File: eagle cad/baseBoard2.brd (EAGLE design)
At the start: 100 x 69.5 mm, 75 parts

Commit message: .
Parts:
- added E$76: 100K, ref-packages:0207/12
- added E$77, E$78: (no value), testpad:P1-13
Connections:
- net GND: now also E$76.1
- net S$22: now also E$76.2
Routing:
- net S$22: track 43.5 -> 45.4 mm
- net GND: track 274.2 -> 275.8 mm
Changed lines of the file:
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@@
 <?xml version="1.0" encoding="utf-8"?>
 <!DOCTYPE eagle SYSTEM "eagle.dtd">
-<eagle version="8.2.2">
+<eagle version="9.6.2">
 <drawing>
 <settings>
 <setting alwaysvectorfont="no"/>
+<setting keepoldvectorfont="yes"/>
 <setting verticaltext="up"/>
 </settings>
-<grid distance="0.2" unitdist="mm" unit="mm" style="lines" multiple="1" display="yes" altdistance="0.003125" altunitdist="mic" altunit="mm"/>
+<grid distance="0.4" unitdist="mm" unit="mm" style="lines" multiple="1" display="yes" altdistance="0.003125" altunitdist="mic" altunit="mm"/>
 <layers>
 <layer number="1" name="Top" color="4" fill="1" visible="yes" active="yes"/>
@@
 <layer number="17" name="Pads" color="2" fill="1" visible="yes" active="yes"/>
 <layer number="18" name="Vias" color="2" fill="1" visible="yes" active="yes"/>
-<layer number="19" name="Unrouted" color="6" fill="1" visible="no" active="yes"/>
+<layer number="19" name="Unrouted" color="6" fill="1" visible="yes" active="yes"/>
 <layer number="20" name="Dimension" color="15" fill="1" visible="yes" active="yes"/>
-<layer number="21" name="tPlace" color="7" fill="1" visible="no" active="yes"/>
+<layer number="21" name="tPlace" color="7" fill="1" visible="yes" active="yes"/>
 <layer number="22" name="bPlace" color="7" fill="1" visible="no" active="yes"/>
-<layer number="23" name="tOrigins" color="15" fill="1" visible="no" active="yes"/>
-<layer number="24" name="bOrigins" color="15" fill="1" visible="no" active="yes"/>
+<layer number="23" name="tOrigins" color="15" fill="1" visible="yes" active="yes"/>
+<layer number="24" name="bOrigins" color="15" fill="1" visible="yes" active="yes"/>
 <layer number="25" name="tNames" color="7" fill="1" visible="no" active="yes"/>
 <layer number="26" name="bNames" color="7" fill="1" visible="no" active="yes"/>
-<layer number="27" name="tValues" color="7" fill="1" visible="no" active="yes"/>
+<layer number="27" name="tValues" color="7" fill="1" visible="yes" active="yes"/>
 <layer number="28" name="bValues" color="7" fill="1" visible="no" active="yes"/>
 <layer number="29" name="tStop" color="7" fill="3" visible="no" active="yes"/>
@@
 <param name="dpMaxLengthDifference" value="10mm"/>
 <param name="dpGapFactor" value="2.5"/>
-<param name="checkGrid" value="0"/>
 <param name="checkAngle" value="0"/>
 <param name="checkFont" value="1"/>
 <param name="checkRestrict" value="1"/>
+<param name="checkStop" value="0"/>
+<param name="checkValues" value="0"/>
+<param name="checkNames" value="1"/>
+<param name="checkWireStubs" value="1"/>
+<param name="checkPolygonWidth" value="0"/>
 <param name="useDiameter" value="13"/>
 <param name="maxErrors" value="50"/>
@@
 <attribute name="VALUE" x="89.2" y="22.6" size="0.0254" layer="27"/>
 </element>
+<element name="E$76" library="ref-packages" library_urn="urn:adsk.eagle:library:338" package="0207/12" value="100K" x="40.8" y="10.4" smashed="yes" rot="R90">
+<attribute name="NAME" x="39.403" y="7.225" size="1.27" layer="25" ratio="10" rot="R90"/>
+<attribute name="VALUE" x="41.4858" y="8.114" size="1.27" layer="27" ratio="10" rot="R90"/>
+</element>
+<element name="E$77" library="testpad" library_urn="urn:adsk.eagle:library:385" package="P1-13" value="" x="40.8" y="16.6" smashed="yes">
+<attribute name="NAME" x="39.784" y="17.87" size="1.27" layer="25" ratio="10"/>
+<attribute name="VALUE" x="40.8" y="16.6" size="0.0254" layer="27"/>
+</element>
+<element name="E$78" library="testpad" library_urn="urn:adsk.eagle:library:385" package="P1-13" value="" x="40.8" y="4.2" smashed="yes">
+<attribute name="NAME" x="39.784" y="5.47" size="1.27" layer="25" ratio="10"/>
+<attribute name="VALUE" x="40.8" y="4.2" size="0.0254" layer="27"/>
+</element>
 </elements>
 <signals>
@@
 <wire x1="58.07" y1="5.6" x2="64.302" y2="5.6" width="1.27" layer="16"/>
 <wire x1="20.62" y1="3.38" x2="21.42" y2="2.58" width="1.27" layer="16"/>
-<wire x1="45.09573125" y1="2.58" x2="21.42" y2="2.58" width="1.27" layer="16"/>
+<wire x1="45.09573125" y1="2.58" x2="41.2" y2="2.58" width="1.27" layer="16"/>
+<wire x1="41.2" y1="2.58" x2="21.42" y2="2.58" width="1.27" layer="16"/>
 <wire x1="45.09573125" y1="2.58" x2="45.13573125" y2="2.54" width="1.27" layer="16"/>
 <wire x1="45.2" y1="2.584" x2="51.6751625" y2="2.584" width="1.27" layer="16"/>
@@
 <wire x1="49.17" y1="19.3" x2="49.37" y2="19.1" width="1.7" layer="16" curve="4.255771"/>
 <wire x1="49.37" y1="19.1" x2="49.27" y2="14.4" width="1.7" layer="16"/>
-<wire x1="74.58" y1="5.73" x2="80.5" y2="16.05" width="0" layer="19" extent="16-16"/>
-<wire x1="64.302" y1="5.6" x2="63" y2="5.55" width="0" layer="19" extent="16-16"/>
+<contactref element="E$76" pad="1"/>
+<wire x1="40.8" y1="4.05" x2="40.8" y2="2.98" width="1.27" layer="16"/>
+<wire x1="40.8" y1="2.98" x2="41.2" y2="2.58" width="0.7" layer="16"/>
+<wire x1="74.58" y1="5.73" x2="80.5" y2="16.05" width="0" layer="19" extent="1-1"/>
+<wire x1="64.42" y1="5.73" x2="63" y2="5.55" width="0" layer="19" extent="16-16"/>
 </signal>
 <signal name="S$5">
@@
 <wire x1="85.9" y1="16.19" x2="85.9" y2="22.63" width="1.27" layer="16"/>
 <contactref element="E$20" pad="+"/>
-<wire x1="45.53" y1="10.16" x2="31.49" y2="10.16" width="1.27" layer="16"/>
+<wire x1="45.53" y1="9.76" x2="31.63" y2="9.76" width="1.27" layer="16"/>
+<wire x1="31.4" y1="9.99" x2="31.63" y2="9.76" width="1.27" layer="16"/>
 <contactref element="E$17" pad="1"/>
-<wire x1="31.49" y1="10.16" x2="31.4" y2="9.99" width="0.7" layer="16"/>
 <wire x1="46.63" y1="19.3" x2="46.63" y2="14.5" width="1.7" layer="16"/>
 <wire x1="46.63" y1="14.5" x2="46.73" y2="14.4" width="0.8128" layer="16"/>
 <wire x1="46.73" y1="14.4" x2="45.53" y2="13.2" width="1.27" layer="16"/>
-<wire x1="45.53" y1="13.2" x2="45.53" y2="10.16" width="1.27" layer="16"/>
+<wire x1="45.53" y1="13.2" x2="45.53" y2="9.76" width="1.27" layer="16"/>
 <wire x1="51.37" y1="39.6" x2="50.97" y2="39.2" width="1.27" layer="16"/>
 <wire x1="50.97" y1="39.2" x2="49.37" y2="37.6" width="1.27" layer="16"/>
@@
 <contactref element="E$46" pad="+"/>
 <contactref element="E$19" pad="4"/>
-<wire x1="45.2" y1="4.616" x2="43.606" y2="6.21" width="1.27" layer="16"/>
-<wire x1="43.606" y1="6.21" x2="28.8" y2="6.21" width="1.27" layer="16"/>
-<wire x1="39.00875" y1="12.8" x2="28.8" y2="12.8" width="1.27" layer="16"/>
-<wire x1="28.8" y1="12.8" x2="28.8" y2="6.21" width="1.27" layer="16"/>
-<wire x1="39.00875" y1="12.8" x2="39.01" y2="12.79" width="0.7" layer="16"/>
-<wire x1="39.01" y1="12.79" x2="39.01" y2="22.39" width="1.27" layer="16"/>
+<wire x1="45.2" y1="4.616" x2="43.006" y2="6.81" width="1.27" layer="16"/>
+<wire x1="43.006" y1="6.81" x2="28.8" y2="6.81" width="1.27" layer="16"/>
+<wire x1="37.40875" y1="12.8" x2="28.8" y2="12.8" width="1.27" layer="16"/>
+<wire x1="28.8" y1="12.8" x2="28.8" y2="6.81" width="1.27" layer="16"/>
+<wire x1="37.40875" y1="12.8" x2="37.41" y2="12.79" width="0.7" layer="16"/>
+<wire x1="37.41" y1="12.79" x2="38.2" y2="12.79" width="1.27" layer="16"/>
+<wire x1="38.2" y1="12.79" x2="38.2" y2="17.2" width="1.27" layer="16"/>
+<wire x1="38.2" y1="17.2" x2="38.2" y2="18" width="1.27" layer="16"/>
+<wire x1="38.2" y1="18" x2="39.01" y2="18.81" width="1.27" layer="16"/>
+<wire x1="39.01" y1="18.81" x2="39.01" y2="22.39" width="1.27" layer="16"/>
+<contactref element="E$76" pad="2"/>
+<wire x1="40.8" y1="16.75" x2="38.65" y2="16.75" width="1.27" layer="16"/>
+<wire x1="38.65" y1="16.75" x2="38.2" y2="17.2" width="0.7" layer="16"/>
 </signal>
 <signal name="S$10">
@@
 </signal>
 </signals>
+<mfgpreviewcolors>
+<mfgpreviewcolor name="soldermaskcolor" color="0xC8008000"/>
+<mfgpreviewcolor name="silkscreencolor" color="0xFFFEFEFE"/>
+<mfgpreviewcolor name="backgroundcolor" color="0xFF282828"/>
+<mfgpreviewcolor name="coppercolor" color="0xFFFFBF00"/>
+<mfgpreviewcolor name="substratecolor" color="0xFF786E46"/>
+</mfgpreviewcolors>
 </board>
 </drawing>
 <compatibility>
 <note version="8.2" severity="warning">
-Since Version 8.2, Eagle supports online libraries. The ids
+Since Version 8.2, EAGLE supports online libraries. The ids
 of those online libraries will not be understood (or retained)
 with this version.

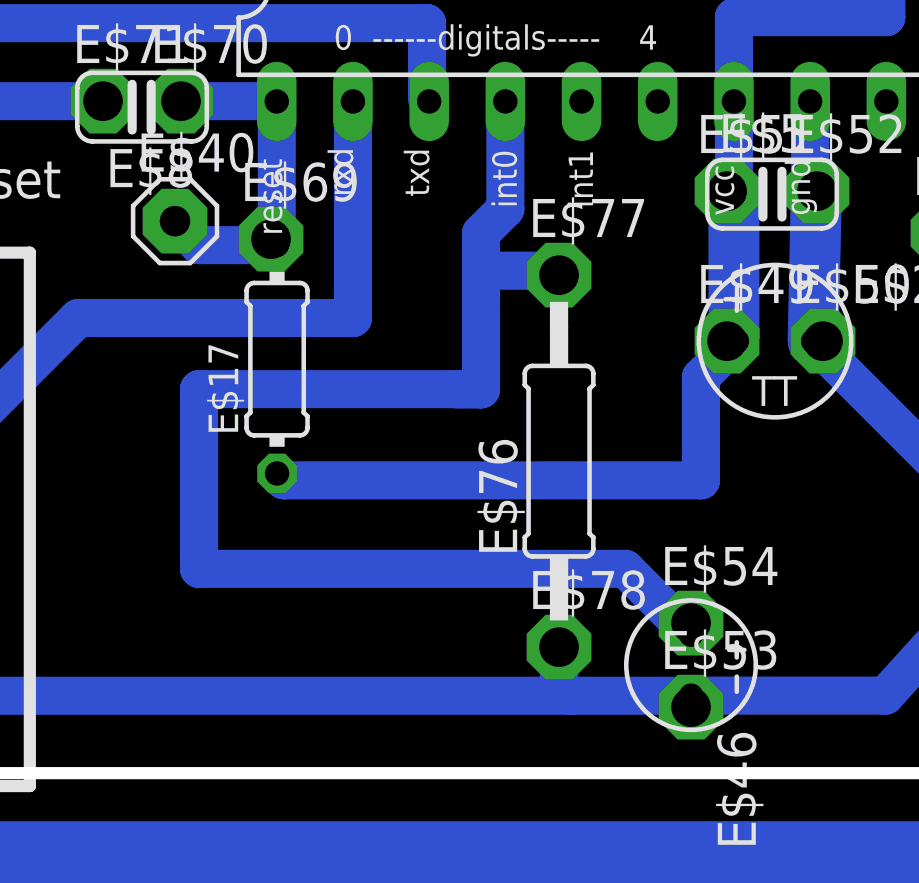
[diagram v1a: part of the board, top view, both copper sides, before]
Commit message: modified pullup resistor for interrupt
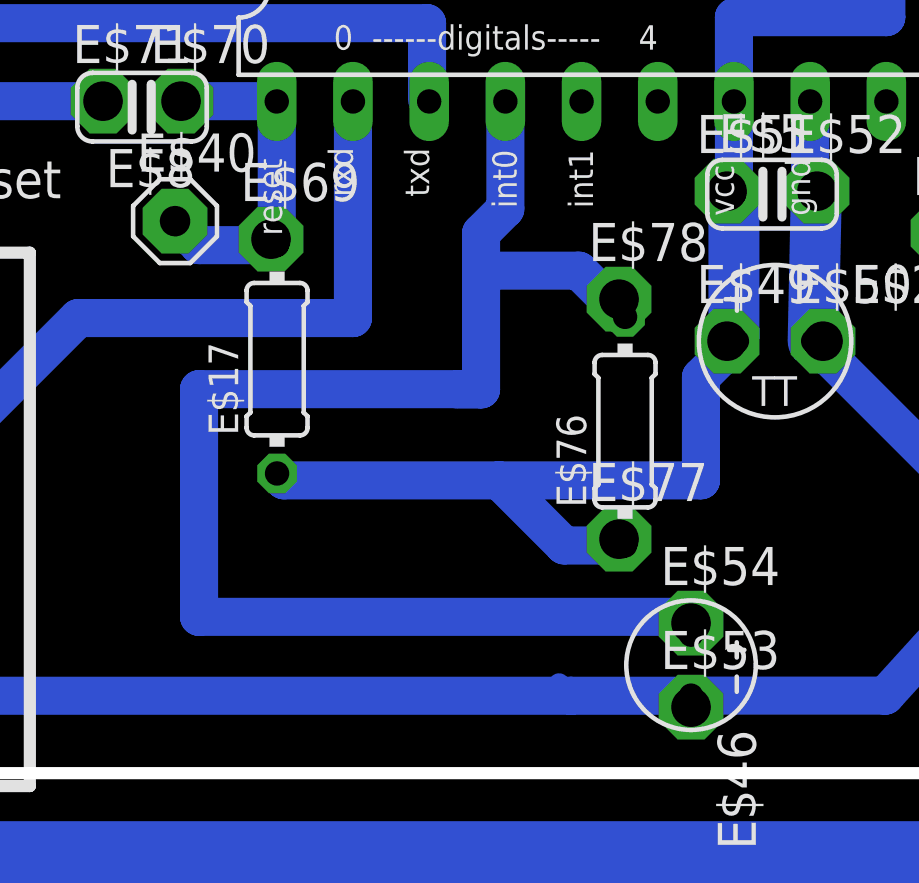
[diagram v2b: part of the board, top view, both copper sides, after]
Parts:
- E$76: value 100K -> 10k; device ref-packages:0207/12 -> eagle-ltspice:0204/7
- moved E$78 11.8 mm to (42.8, 15.8)
- moved E$77 9.02 mm to (42.8, 7.80)
- moved E$76 2.42 mm to (43.0, 11.4)
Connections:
- net GND: no longer E$76.1
- net VCC3.3V: now also E$76.1
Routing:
- net VCC3.3V: track 133.9 -> 139.0 mm
- net S$22: track 45.4 -> 49.2 mm
- net GND: track 275.8 -> 274.7 mm
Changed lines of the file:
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@@
 <attribute name="VALUE" x="89.2" y="22.6" size="0.0254" layer="27"/>
 </element>
-<element name="E$76" library="ref-packages" library_urn="urn:adsk.eagle:library:338" package="0207/12" value="100K" x="40.8" y="10.4" smashed="yes" rot="R90">
-<attribute name="NAME" x="39.403" y="7.225" size="1.27" layer="25" ratio="10" rot="R90"/>
-<attribute name="VALUE" x="41.4858" y="8.114" size="1.27" layer="27" ratio="10" rot="R90"/>
+<element name="E$77" library="testpad" library_urn="urn:adsk.eagle:library:385" package="P1-13" value="" x="42.8" y="7.8" smashed="yes">
+<attribute name="NAME" x="41.784" y="9.07" size="1.27" layer="25" ratio="10"/>
+<attribute name="VALUE" x="42.8" y="7.8" size="0.0254" layer="27"/>
 </element>
-<element name="E$77" library="testpad" library_urn="urn:adsk.eagle:library:385" package="P1-13" value="" x="40.8" y="16.6" smashed="yes">
-<attribute name="NAME" x="39.784" y="17.87" size="1.27" layer="25" ratio="10"/>
-<attribute name="VALUE" x="40.8" y="16.6" size="0.0254" layer="27"/>
+<element name="E$78" library="testpad" library_urn="urn:adsk.eagle:library:385" package="P1-13" value="" x="42.8" y="15.8" smashed="yes">
+<attribute name="NAME" x="41.784" y="17.07" size="1.27" layer="25" ratio="10"/>
+<attribute name="VALUE" x="42.8" y="15.8" size="0.0254" layer="27"/>
 </element>
-<element name="E$78" library="testpad" library_urn="urn:adsk.eagle:library:385" package="P1-13" value="" x="40.8" y="4.2" smashed="yes">
-<attribute name="NAME" x="39.784" y="5.47" size="1.27" layer="25" ratio="10"/>
-<attribute name="VALUE" x="40.8" y="4.2" size="0.0254" layer="27"/>
+<element name="E$76" library="eagle-ltspice" package="0204/7" value="10k" x="43" y="11.4" smashed="yes" rot="R90">
+<attribute name="NAME" x="41.7046" y="8.86" size="0.9906" layer="25" ratio="10" rot="R90"/>
+<attribute name="VALUE" x="43.4826" y="10.6744" size="0.9906" layer="27" ratio="10" rot="R90"/>
 </element>
 </elements>
@@
 <wire x1="49.17" y1="19.3" x2="49.37" y2="19.1" width="1.7" layer="16" curve="4.255771"/>
 <wire x1="49.37" y1="19.1" x2="49.27" y2="14.4" width="1.7" layer="16"/>
-<contactref element="E$76" pad="1"/>
-<wire x1="40.8" y1="4.05" x2="40.8" y2="2.98" width="1.27" layer="16"/>
 <wire x1="40.8" y1="2.98" x2="41.2" y2="2.58" width="0.7" layer="16"/>
 <wire x1="74.58" y1="5.73" x2="80.5" y2="16.05" width="0" layer="19" extent="1-1"/>
@@
 <wire x1="85.9" y1="16.19" x2="85.9" y2="22.63" width="1.27" layer="16"/>
 <contactref element="E$20" pad="+"/>
-<wire x1="45.53" y1="9.76" x2="31.63" y2="9.76" width="1.27" layer="16"/>
+<wire x1="45.53" y1="9.76" x2="38.8" y2="9.76" width="1.27" layer="16"/>
+<wire x1="38.8" y1="9.76" x2="31.63" y2="9.76" width="1.27" layer="16"/>
 <wire x1="31.4" y1="9.99" x2="31.63" y2="9.76" width="1.27" layer="16"/>
 <contactref element="E$17" pad="1"/>
@@
 <wire x1="50.8" y1="39.4" x2="50.8" y2="39.37" width="0.7" layer="16"/>
 <wire x1="50.8" y1="39.37" x2="50.97" y2="39.2" width="0.7" layer="16"/>
+<contactref element="E$76" pad="1"/>
+<wire x1="43" y1="7.59" x2="40.97" y2="7.59" width="1.27" layer="16"/>
+<wire x1="40.97" y1="7.59" x2="38.8" y2="9.76" width="1.27" layer="16"/>
 </signal>
 <signal name="S$3">
@@
 <contactref element="E$46" pad="+"/>
 <contactref element="E$19" pad="4"/>
-<wire x1="45.2" y1="4.616" x2="43.006" y2="6.81" width="1.27" layer="16"/>
-<wire x1="43.006" y1="6.81" x2="28.8" y2="6.81" width="1.27" layer="16"/>
+<wire x1="45.2" y1="4.616" x2="44.606" y2="5.21" width="1.27" layer="16"/>
+<wire x1="44.606" y1="5.21" x2="28.8" y2="5.21" width="1.27" layer="16"/>
 <wire x1="37.40875" y1="12.8" x2="28.8" y2="12.8" width="1.27" layer="16"/>
-<wire x1="28.8" y1="12.8" x2="28.8" y2="6.81" width="1.27" layer="16"/>
+<wire x1="28.8" y1="12.8" x2="28.8" y2="5.21" width="1.27" layer="16"/>
 <wire x1="37.40875" y1="12.8" x2="37.41" y2="12.79" width="0.7" layer="16"/>
 <wire x1="37.41" y1="12.79" x2="38.2" y2="12.79" width="1.27" layer="16"/>
@@
 <wire x1="38.2" y1="18" x2="39.01" y2="18.81" width="1.27" layer="16"/>
 <wire x1="39.01" y1="18.81" x2="39.01" y2="22.39" width="1.27" layer="16"/>
+<wire x1="41.46" y1="16.75" x2="38.65" y2="16.75" width="1.27" layer="16"/>
+<wire x1="38.65" y1="16.75" x2="38.2" y2="17.2" width="0.7" layer="16"/>
 <contactref element="E$76" pad="2"/>
-<wire x1="40.8" y1="16.75" x2="38.65" y2="16.75" width="1.27" layer="16"/>
-<wire x1="38.65" y1="16.75" x2="38.2" y2="17.2" width="0.7" layer="16"/>
+<wire x1="43" y1="15.21" x2="41.46" y2="16.75" width="1.27" layer="16"/>
 </signal>
 <signal name="S$10">
